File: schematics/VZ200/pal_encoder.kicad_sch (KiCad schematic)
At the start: 76 parts, among them Q1 1402D, Q1 1502C, Q1 NA31X, U907 74LS123, U908 TBA520, Y902 4.43MHz

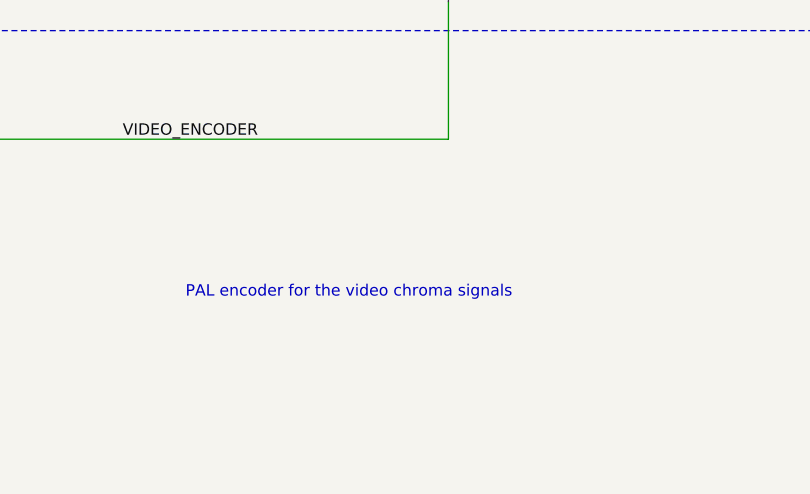
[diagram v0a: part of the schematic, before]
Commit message: Schematic for the VZ200 printer interface
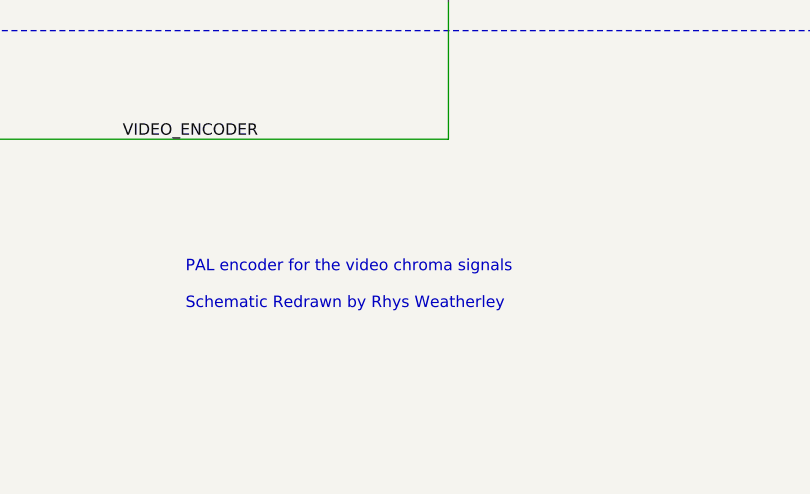
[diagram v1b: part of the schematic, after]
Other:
- note added: "PAL encoder for the video chroma signals Schematic Redrawn by Rhys Weatherley"
- note removed: "PAL encoder for the video chroma signals"
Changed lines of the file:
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@@
     (effects (font (size 1.27 1.27)) (justify left bottom))
   )
-  (text "PAL encoder for the video chroma signals" (at 184.785 175.26 0)
+  (text "PAL encoder for the video chroma signals\n\nSchematic Redrawn by Rhys Weatherley"
+    (at 184.785 176.53 0)
     (effects (font (size 1.27 1.27)) (justify left bottom))
   )

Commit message: Add title and revision details to the schematic sheets
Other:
- title: (none) -> VZ200 Computer
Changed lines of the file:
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@@
 (kicad_sch (version 20230121) (generator eeschema)
   (paper "A4")
+  (title_block
+    (title "VZ200 Computer")
+    (date "2024-01-01")
+    (rev "1")
+  )
   (junction (at 182.245 84.455) (diameter 0) (color 0 0 0 0)
   )

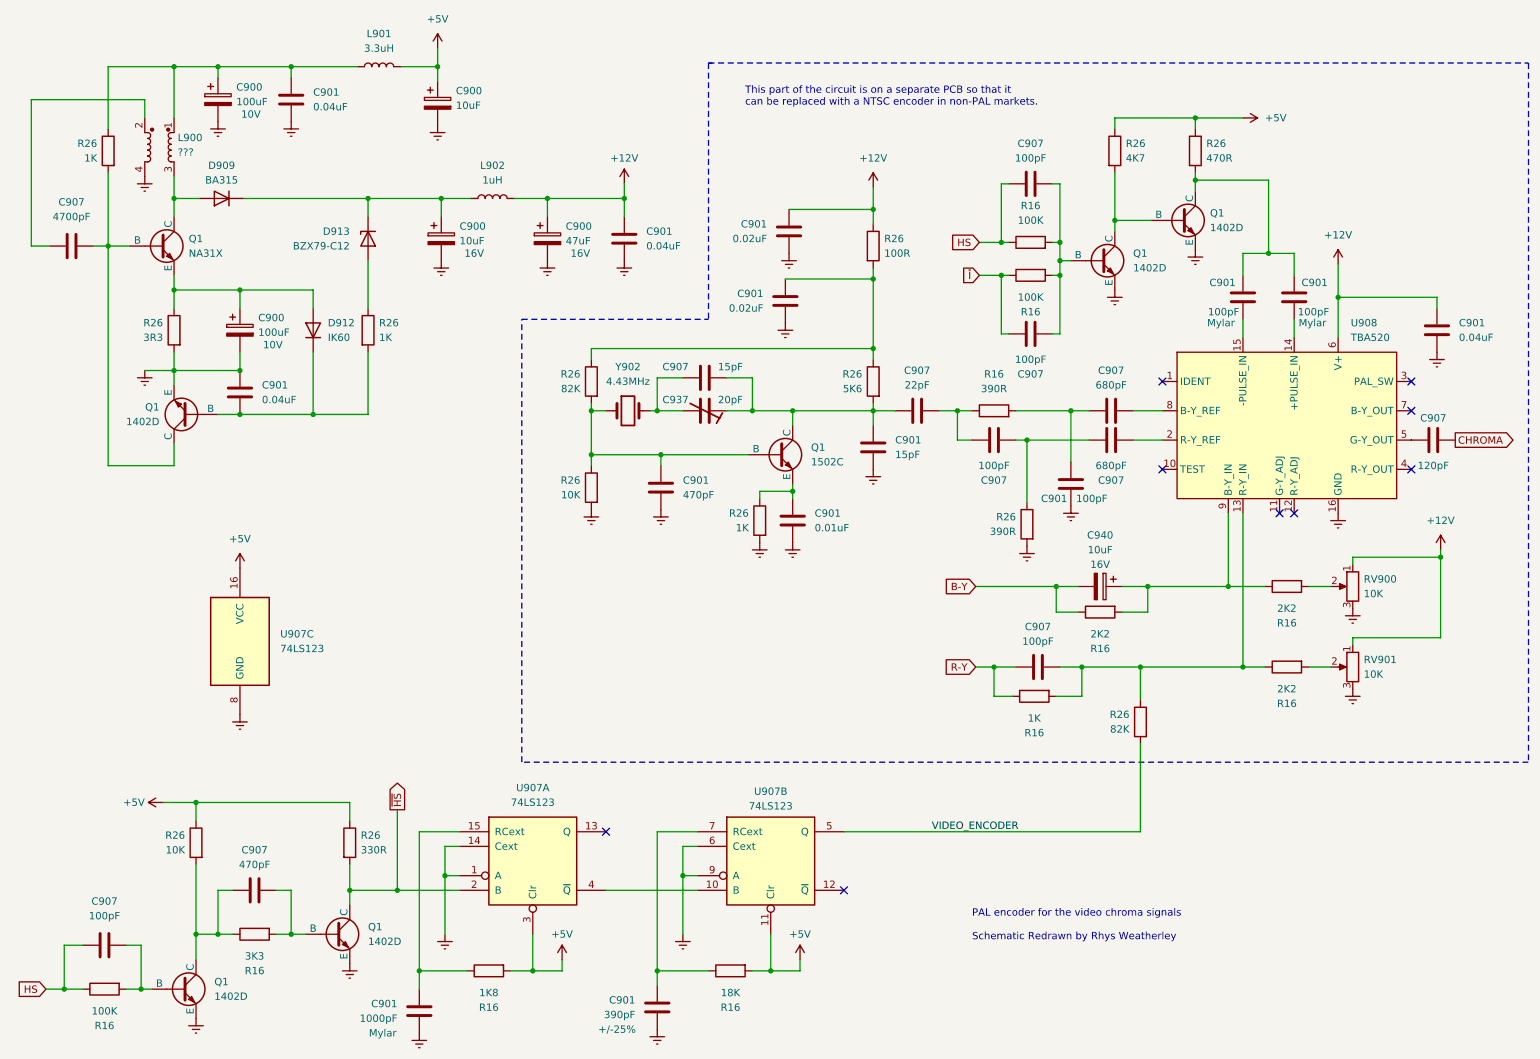
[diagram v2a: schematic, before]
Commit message: Update motherboard schematic based on inspection of the actual board
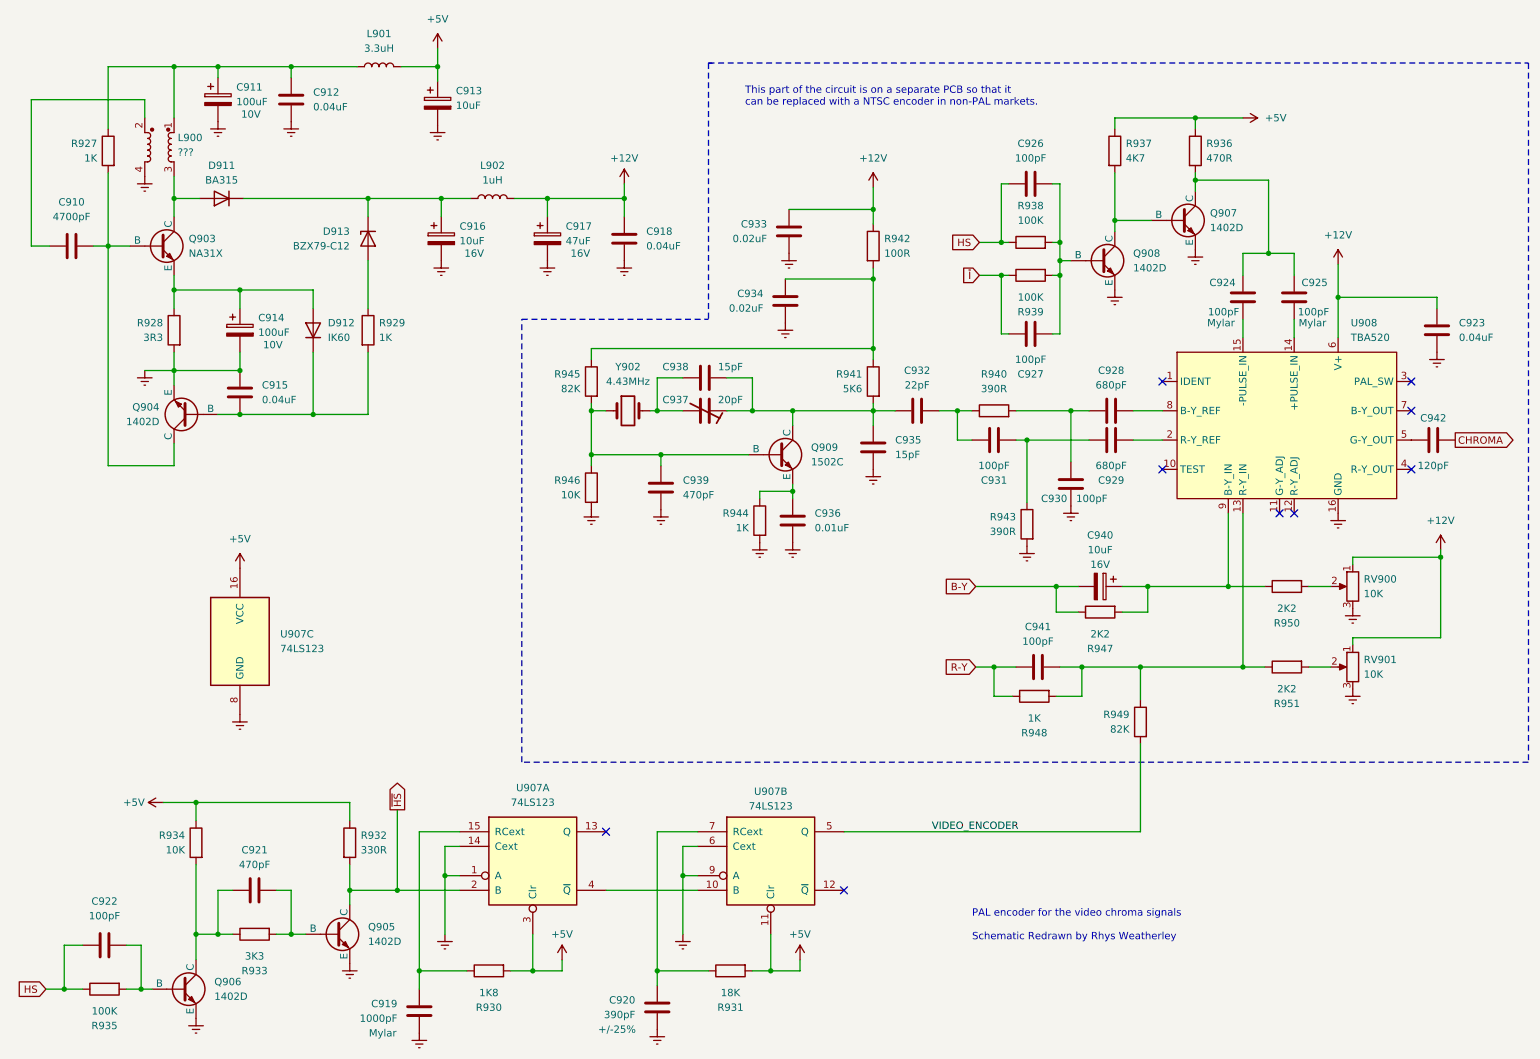
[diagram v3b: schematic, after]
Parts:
- renumbered C907 to C910, C900 to C911, C901 to C912, C900 to C913, C900 to C914, C901 to C915, C900 to C916, C900 to C917, C901 to C918, C901 to C919, C901 to C920, C907 to C921, C907 to C922, C901 to C923, C901 to C924, C901 to C925, C907 to C926, C907 to C927, C907 to C928, C907 to C929, C901 to C930, C907 to C931, C907 to C932, C901 to C933, C901 to C934, C901 to C935, C901 to C936, C907 to C938, C901 to C939, C907 to C941, C907 to C942, D909 to D911, Q1 to Q903, Q1 to Q904, Q1 to Q905, Q1 to Q906, Q1 to Q907, Q1 to Q908, Q1 to Q909, R26 to R927, R26 to R928, R26 to R929, R16 to R930, R16 to R931, R26 to R932, R16 to R933, R26 to R934, R16 to R935, R26 to R936, R26 to R937, R16 to R938, R16 to R939, R16 to R940, R26 to R941, R26 to R942, R26 to R943, R26 to R944, R26 to R945, R26 to R946, R16 to R947, R16 to R948, R26 to R949, R16 to R950, R16 to R951
